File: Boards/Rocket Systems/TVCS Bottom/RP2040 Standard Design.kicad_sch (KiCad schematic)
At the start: 40 parts, among them J2 BM03B-SRSS-TBLFSN, J4 DX07S016JA1R1500, U1 ST1L05APU33R, U2 W25Q128JVSIQ TR, U3 ESD7L5.0DT5G

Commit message: Repo Refactor and new systems update
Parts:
- removed CV31, CV35: 1uF, Capacitor_0402:Capacitor_0402, symbol Device:C
- removed CV32, CV36: 100nF, Capacitor_0402:Capacitor_0402, symbol Device:C
- removed CV33, CV34: 4.7uF, C_4uF7_0402:C_4uF7_0402, symbol Device:C
- removed D1: PMEG2010ER, PMEG2010ER:SODFL3517X110N, symbol Schottky Diode:PMEG2010ER
- removed J2: BM03B-SRSS-TBLFSN, SWD_Con:CONN_BM03B-SRSS-TBLFSN_JST, symbol SWD Connector:BM03B-SRSS-TBLFSN
- removed J4: DX07S016JA1R1500, USBC-DX07S016JA1:JAE_DX07S016JA1R1500, symbol DX07S016JA1R1500:DX07S016JA1R1500
- removed R1, R10, R17: 1k, RES_0402:RES_0402, symbol Device:R
- removed R16: 10k, RES_0402:RES_0402, symbol Device:R
- removed R18, RC2: 5k1, R_0805_5K1:R_0805_5K1, symbol Device:R
- removed R2: 650, RC0402N_VIS:RC0402N_VIS, symbol Device:R
- removed R6, R7: 27, RES_R0603_27:RES_R0603_27, symbol Device:R
- removed R8, R9: 100, RES_0402:RES_0402, symbol Device:R
- removed U1: ST1L05APU33R, LDO ST1L05A:DFN_5APU33R_STM, symbol LDO 5V 3V3:ST1L05APU33R
- removed U2: W25Q128JVSIQ TR, NOR Flash:SOIC_208MIL_WIN, symbol 16MB Flash Memory:W25Q128JVSIQ_TR
- removed U3: ESD7L5.0DT5G, ESD7L5-Diode:SOT-723_0P85X1P25_ONS, symbol ESD Diodes:ESD7L5.0DT5G
- removed XTAL1: ASE-12.000MHZ-LC-T, AS12MHz:ASE-3.2X2.5_ABR, symbol Powered Crystal:ASE-12.000MHZ-LC-T
- added CV13, CV17: 1uF, Capacitor_0402:Capacitor_0402, symbol Device:C
- added CV14, CV18: 100nF, Capacitor_0402:Capacitor_0402, symbol Device:C
- added CV15, CV16: 4.7uF, C_4uF7_0402:C_4uF7_0402, symbol Device:C
- added D2: PMEG2010ER, PMEG2010ER:SODFL3517X110N, symbol PMEG2010ER:PMEG2010ER
- added J16: DX07S016JA1R1500, DX07S016JA1R1500:JAE_DX07S016JA1R1500, symbol DX07S016JA1R1500:DX07S016JA1R1500
- added J7: BM03B-SRSS-TBLFSN, CONN_BM03B-SRSS-TBLFSN_JST, symbol SWD_Con:BM03B-SRSS-TBLFSN
- added R22, R23: 27, RES_R0603_27:RES_R0603_27, symbol Device:R
- added R24, R25: 100, RES_0402:RES_0402, symbol Device:R
- added R26, R3, R35: 1k, RES_0402:RES_0402, symbol Device:R
- added R29: 10k, RES_0402:RES_0402, symbol Device:R
- added R30: 650, symbol Device:R
- added R33, R36: 5k1, R_0805_5K1:R_0805_5K1, symbol Device:R
- added U2: W25Q128JVSIQ TR, SOIC_208MIL_WIN, symbol 16MB_Flash:W25Q128JVSIQ_TR
- added U6: ESD7L5.0DT5G, SOT-723_0P85X1P25_ONS, symbol ESD7L5_Diode:ESD7L5.0DT5G
- added U7: ST1L05APU33R, DFN_5APU33R_STM, symbol LDO_ST1L05A:ST1L05APU33R
- added XTAL1: ASE-12.000MHZ-LC-T, ASE-3.2X2.5_ABR, symbol AS12MHz:ASE-12.000MHZ-LC-T
- S1, S2: footprint E-Switch_7mm:SW_TL3305CF160QG -> TL3305CF160QG:SW_TL3305CF160QG
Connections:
- net +3.3V: now also CV13.1, CV14.1, CV16.2, CV18.1, R29.2, R3.1, U2.8 (VCC), U7.2 (V0), XTAL1.4 (VDD)
- net +5V: now also CV15.2, CV17.2, D2.C, U7.3 (V1)
- net CRYSTAL: now also XTAL1.3 (OUTPUT)
- net GND: now also CV13.2, CV14.2, CV15.1, CV16.1, CV17.1, CV18.2, J16.1 (GND), J16.12 (GND), J7.2, R33.1, R36.1, U2.4 (GND), U6.3, U7.6 (GND), U7.7 (GND), XTAL1.2 (GND/CASE)
- net MCU QSPI_SCLK: now also U2.6 (CLK)
- net MCU QSPI_SD0: now also U2.5 (DI(IO0))
- net MCU QSPI_SD1: now also U2.2 (DO(IO1))
- net MCU QSPI_SD2: now also U2.3 (/WP(IO2))
- net MCU QSPI_SD3: now also U2.7 (/HOLD_/RESET)
- net MCU QSPI_SS: now also R35.2, U2.1 (/CS)
- net USB_DM: now also J16.5 (D-), J16.8 (D-), R23.1, U6.1
- net USB_DP: now also J16.6 (D+), J16.7 (D+), R22.1, U6.2
- net ~{RST}: now also S1.4, R26.1; no longer S2.4
- net ~{USB_BOOT}: now also S2.4, R35.1; no longer S1.4
- net at MCU1.47 (USB_DP): now also R22.2
- net at MCU1.25 (SWD): now also R25.2
- net at MCU1.24 (SWCLK): now also R24.2
- net at CV1.1, MCU1.26 (RUN): now also R26.2, R3.2
- net at CR1.2: now also R30.2
- net at MCU1.37 (GPIO25): now also R30.1
- net at MCU1.46 (USB_DM): now also R23.2
- net GP10/SPI1 SCK renamed GPIO10
- net GP11/SPI1 MOSI renamed GPIO11
- net GP17/SPI0 ~{CS} renamed GP17/SPI0 ~{CS2}
- net GP21/PWM2 B/CLKOUT 0 renamed GP21/SPI0 ~{CS3}
- net GP22/PWM3 A/CLKIN 1 renamed GPIO22
- net GP23/PWM3 B/CLKOUT 1 renamed GPIO23
- net GP3/UART0 RTS renamed GPIO3
- net GP4/UART1 TX renamed GPIO4
- net GP5/UART1 RX renamed GP5/SPI0 ~{CS1}
- net GP6/UART1 CTS renamed GPIO6
- net GP7/UART1 RTS renamed GPIO7
- net GP9/SPI1 ~{CS} renamed GPIO9
- new net: D2.A, J16.11 (VBUS), J16.2 (VBUS)
- new net: J16.3 (CC1), R36.2
- new net: J16.9 (CC2), R33.2
- new net: J16.S1 (SHIELD), J16.S2 (SHIELD), J16.S3 (SHIELD), J16.S4 (SHIELD), J16.S5 (SHIELD), J16.S6 (SHIELD)
- new net: J7.1, R24.1
- new net: J7.3, R25.1
- new net: R29.1, XTAL1.1 (TRI-STATE(STBY))

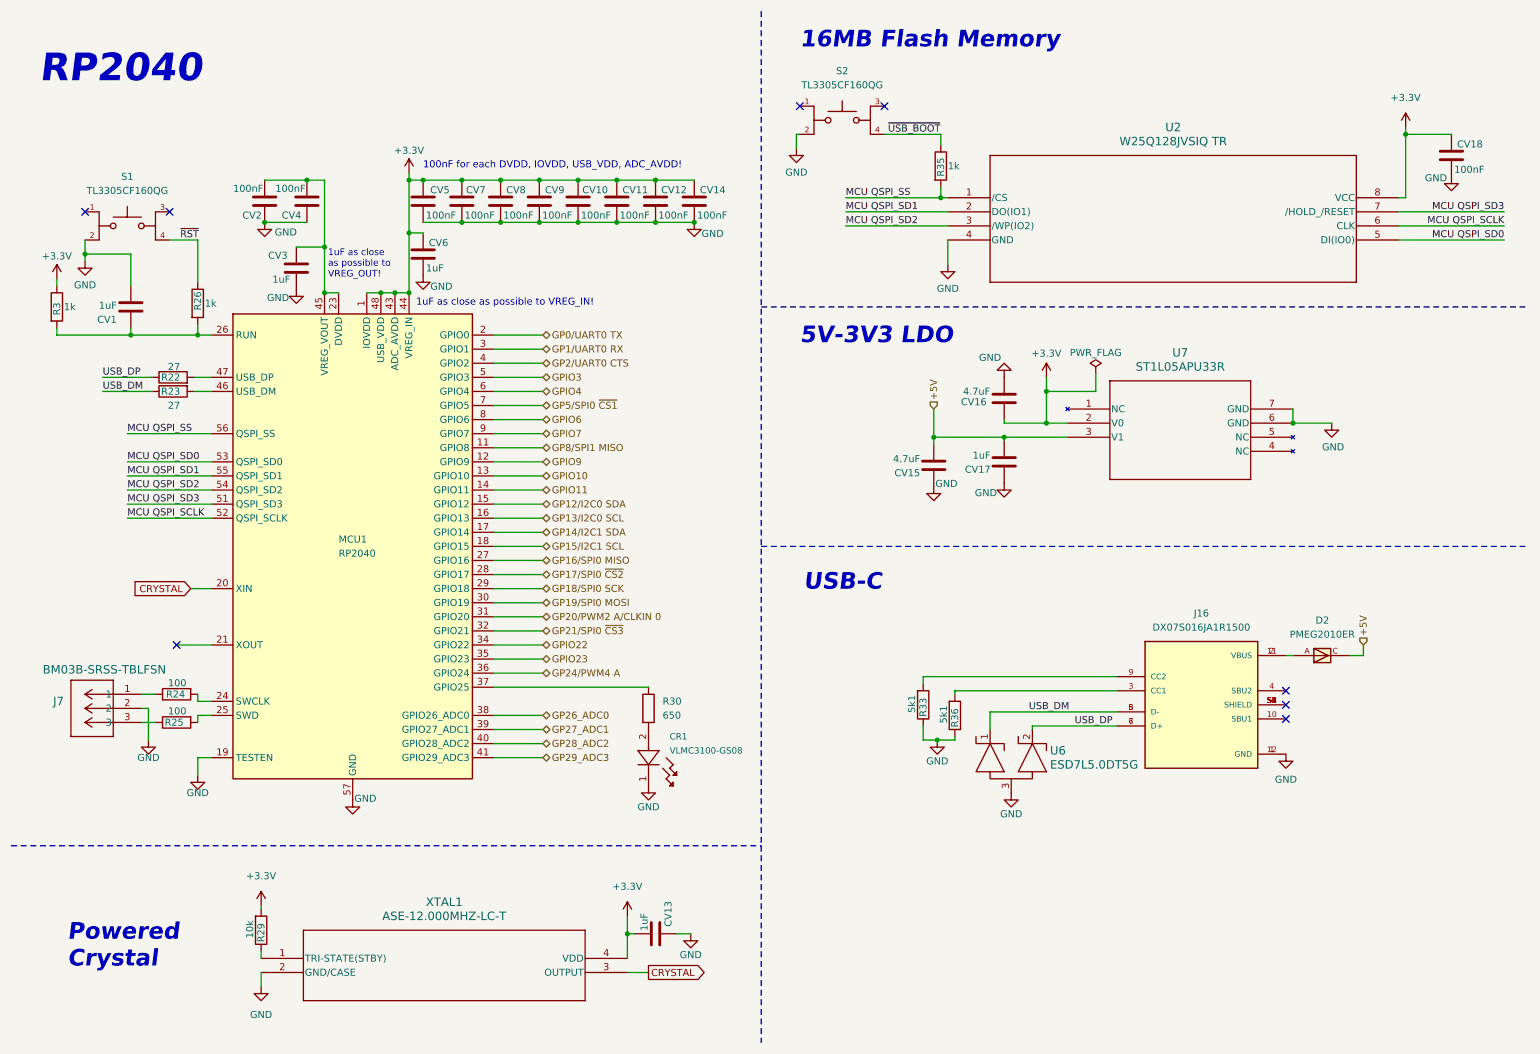
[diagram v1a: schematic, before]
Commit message: TVCS Top and Bottom
Footprints atualizadas
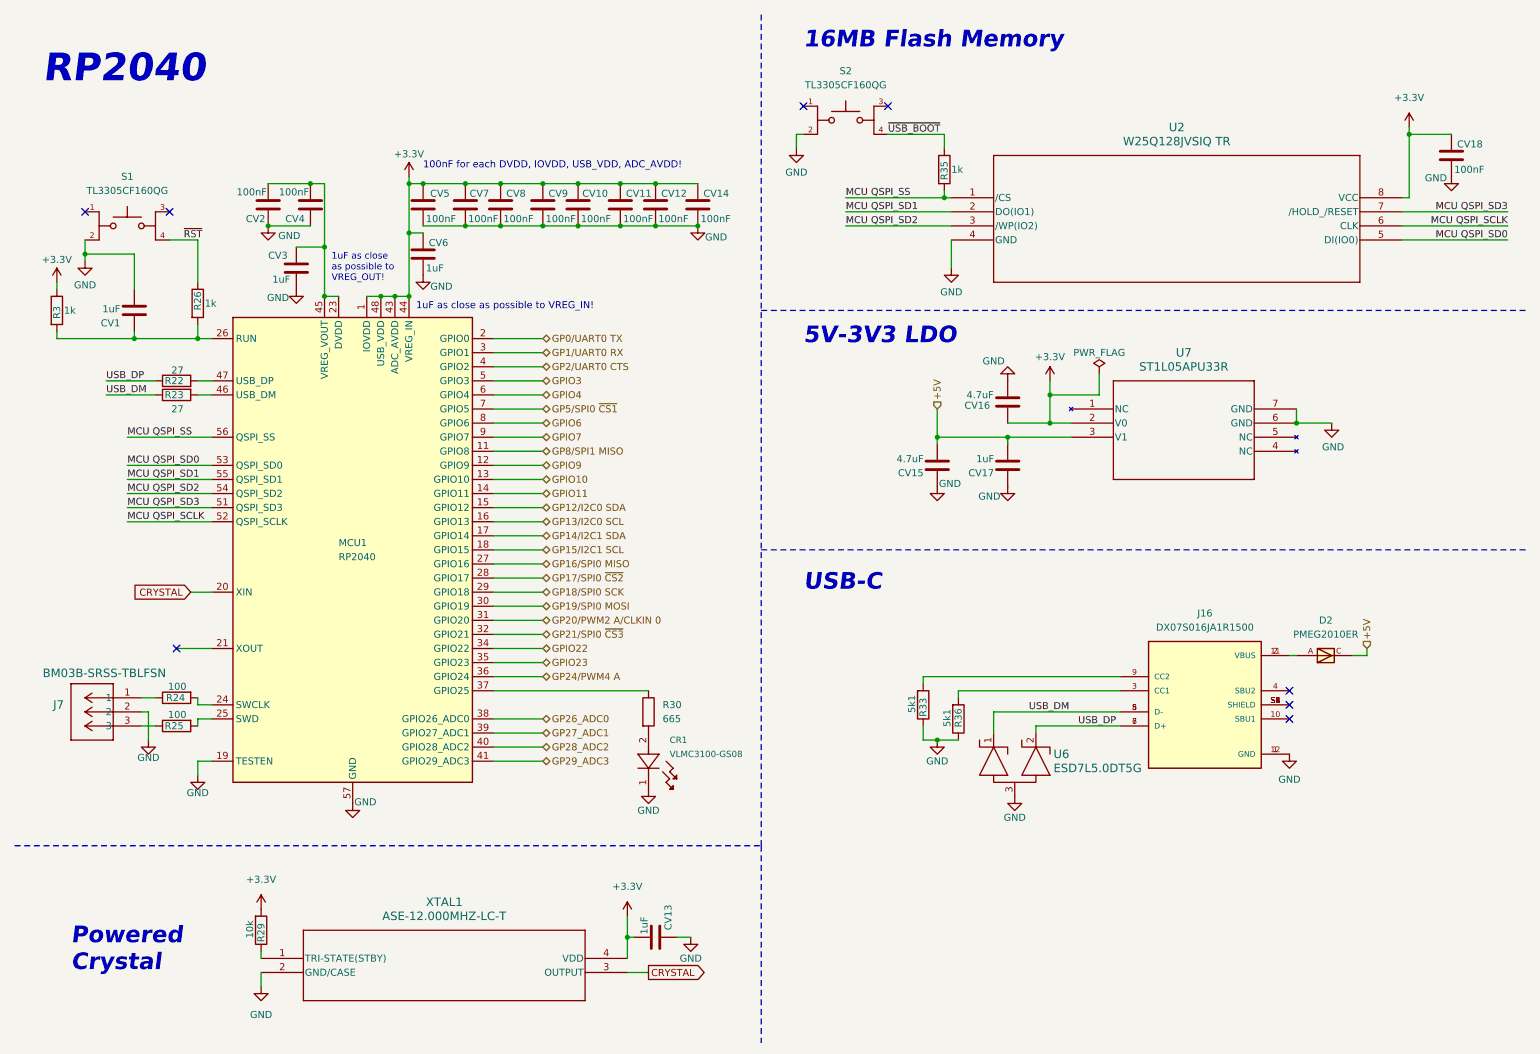
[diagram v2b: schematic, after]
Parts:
- CR1: footprint LED_PLCC_VSMB -> LED-Green_VLMC3100-GS08:LED_PLCC_VSMB
- CV1, CV10, CV11, CV12, CV13, CV14, CV17, CV18, CV2, CV3, CV4, CV5, CV6, CV7, CV8, CV9: footprint Capacitor_0402:Capacitor_0402 -> Capacitor-0402:Capacitor_0402
- CV15, CV16: footprint C_4uF7_0402:C_4uF7_0402 -> Capacitor-0402:Capacitor_0402
- D2: footprint PMEG2010ER:SODFL3517X110N -> Diode-Schottky_PMEG2010ER:SODFL3517X110N
- J16: footprint DX07S016JA1R1500:JAE_DX07S016JA1R1500 -> USBC-DX07S016JA1:JAE_DX07S016JA1R1500
- J7: footprint CONN_BM03B-SRSS-TBLFSN_JST -> SWD_Con:CONN_BM03B-SRSS-TBLFSN_JST
- R22, R23: footprint RES_R0603_27:RES_R0603_27 -> Resistor-0603:RES_0603
- R24, R25, R26, R29, R3, R35: footprint RES_0402:RES_0402 -> Resistor-0402:RES_0402
- R30: value 650 -> 665; footprint (none) -> Resistor-0402:RES_0402
- R33, R36: footprint R_0805_5K1:R_0805_5K1 -> Resistor-0805:RES_0805
- S1, S2: footprint TL3305CF160QG:SW_TL3305CF160QG -> E-Switch_7mm:SW_TL3305CF160QG
- U2: footprint SOIC_208MIL_WIN -> NOR Flash:SOIC_208MIL_WIN
- U6: footprint SOT-723_0P85X1P25_ONS -> ESD7L5-Diode:SOT-723_0P85X1P25_ONS
- U7: footprint DFN_5APU33R_STM -> LDO ST1L05A:DFN_5APU33R_STM
- XTAL1: footprint ASE-3.2X2.5_ABR -> AS12MHz:ASE-3.2X2.5_ABR

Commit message: Tu viste o q eu fiz
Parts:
- removed S1, S2: TL3305CF160QG, E-Switch_7mm:SW_TL3305CF160QG, symbol TL3305CF160QG:TL3305CF160QG
- added S1, S2: TL1017AABF160QG, E-Switch_Small:TL1017AABF160QG, symbol TL1017AABF160QG:TL1017AABF160QG
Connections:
- net GND: now also S1.1 (COM), S1.G1, S2.1 (COM), S2.G1
- net ~{RST}: now also S1.2 (NO)
- net ~{USB_BOOT}: now also S2.2 (NO)
- no-connect marks 8 -> 4

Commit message: Communication boards update
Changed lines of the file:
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@@
 	(wire
 		(pts
-			(xy 256.54 128.27) (xy 254 128.27)
+			(xy 258.445 128.27) (xy 254 128.27)
 		)
 		(stroke
@@
 	(wire
 		(pts
-			(xy 256.54 127) (xy 256.54 128.27)
+			(xy 258.445 127) (xy 258.445 128.27)
 		)
 		(stroke
@@
 	(label "MCU QSPI_SS"
 		(at 33.02 88.9 0)
-		(fields_autoplaced yes)
 		(effects
 			(font
@@
 	(label "MCU QSPI_SD3"
 		(at 33.02 101.6 0)
-		(fields_autoplaced yes)
 		(effects
 			(font
@@
 	(label "MCU QSPI_SD1"
 		(at 162.56 48.26 0)
-		(fields_autoplaced yes)
 		(effects
 			(font
@@
 	(label "MCU QSPI_SD0"
 		(at 33.02 93.98 0)
-		(fields_autoplaced yes)
 		(effects
 			(font
@@
 	(label "USB_DM"
 		(at 29.21 81.28 0)
-		(fields_autoplaced yes)
 		(effects
 			(font
@@
 	(label "~{RST}"
 		(at 43.18 52.07 0)
-		(fields_autoplaced yes)
 		(effects
 			(font
@@
 	(label "MCU QSPI_SD2"
 		(at 33.02 99.06 0)
-		(fields_autoplaced yes)
 		(effects
 			(font
@@
 	(label "MCU QSPI_SD3"
 		(at 281.94 48.26 180)
-		(fields_autoplaced yes)
 		(effects
 			(font
@@
 	(label "USB_DM"
 		(at 195.58 138.43 0)
-		(fields_autoplaced yes)
 		(effects
 			(font
@@
 	(label "MCU QSPI_SD0"
 		(at 281.94 53.34 180)
-		(fields_autoplaced yes)
 		(effects
 			(font
@@
 	(label "MCU QSPI_SCLK"
 		(at 281.94 50.8 180)
-		(fields_autoplaced yes)
 		(effects
 			(font
@@
 	(label "USB_DP"
 		(at 29.21 78.74 0)
-		(fields_autoplaced yes)
 		(effects
 			(font
@@
 	(label "MCU QSPI_SS"
 		(at 162.56 45.72 0)
-		(fields_autoplaced yes)
 		(effects
 			(font
@@
 	(label "MCU QSPI_SD1"
 		(at 33.02 96.52 0)
-		(fields_autoplaced yes)
 		(effects
 			(font
@@
 	(label "MCU QSPI_SD2"
 		(at 162.56 50.8 0)
-		(fields_autoplaced yes)
 		(effects
 			(font
@@
 	(label "~{USB_BOOT}"
 		(at 170.18 34.29 0)
-		(fields_autoplaced yes)
 		(effects
 			(font
@@
 	(label "USB_DP"
 		(at 204.47 140.97 0)
-		(fields_autoplaced yes)
 		(effects
 			(font
@@
 	(label "MCU QSPI_SCLK"
 		(at 33.02 104.14 0)
-		(fields_autoplaced yes)
 		(effects
 			(font
@@
 		(shape bidirectional)
 		(at 107.95 142.24 0)
-		(fields_autoplaced yes)
 		(effects
 			(font
@@
 		(shape bidirectional)
 		(at 107.95 96.52 0)
-		(fields_autoplaced yes)
 		(effects
 			(font
@@
 		(shape bidirectional)
 		(at 107.95 106.68 0)
-		(fields_autoplaced yes)
 		(effects
 			(font
@@
 		(shape bidirectional)
 		(at 107.95 83.82 0)
-		(fields_autoplaced yes)
 		(effects
 			(font
@@
 		(shape bidirectional)
 		(at 107.95 147.32 0)
-		(fields_autoplaced yes)
 		(effects
 			(font
@@
 		(shape bidirectional)
 		(at 107.95 76.2 0)
-		(fields_autoplaced yes)
 		(effects
 			(font
@@
 		(shape bidirectional)
 		(at 107.95 71.12 0)
-		(fields_autoplaced yes)
 		(effects
 			(font
@@
 		(shape bidirectional)
 		(at 107.95 119.38 0)
-		(fields_autoplaced yes)
 		(effects
 			(font
@@
 		(shape bidirectional)
 		(at 107.95 124.46 0)
-		(fields_autoplaced yes)
 		(effects
 			(font
@@
 		(shape bidirectional)
 		(at 107.95 93.98 0)
-		(fields_autoplaced yes)
 		(effects
 			(font
@@
 		(shape bidirectional)
 		(at 107.95 88.9 0)
-		(fields_autoplaced yes)
 		(effects
 			(font
@@
 		(shape bidirectional)
 		(at 107.95 101.6 0)
-		(fields_autoplaced yes)
 		(effects
 			(font
@@
 		(shape input)
 		(at 179.07 83.82 90)
-		(fields_autoplaced yes)
 		(effects
 			(font
@@
 		(shape bidirectional)
 		(at 107.95 73.66 0)
-		(fields_autoplaced yes)
 		(effects
 			(font
@@
 		(shape bidirectional)
 		(at 107.95 129.54 0)
-		(fields_autoplaced yes)
 		(effects
 			(font
@@
 		(shape bidirectional)
 		(at 107.95 144.78 0)
-		(fields_autoplaced yes)
 		(effects
 			(font
@@
 		(shape bidirectional)
 		(at 107.95 86.36 0)
-		(fields_autoplaced yes)
 		(effects
 			(font
@@
 		(shape bidirectional)
 		(at 107.95 121.92 0)
-		(fields_autoplaced yes)
 		(effects
 			(font
@@
 		(shape bidirectional)
 		(at 107.95 109.22 0)
-		(fields_autoplaced yes)
 		(effects
 			(font
@@
 		(shape bidirectional)
 		(at 107.95 127 0)
-		(fields_autoplaced yes)
 		(effects
 			(font
@@
 		(shape bidirectional)
 		(at 107.95 91.44 0)
-		(fields_autoplaced yes)
 		(effects
 			(font
@@
 		(shape bidirectional)
 		(at 107.95 78.74 0)
-		(fields_autoplaced yes)
 		(effects
 			(font
@@
 		(shape bidirectional)
 		(at 107.95 132.08 0)
-		(fields_autoplaced yes)
 		(effects
 			(font
@@
 		(shape bidirectional)
 		(at 107.95 104.14 0)
-		(fields_autoplaced yes)
 		(effects
 			(font
@@
 		(shape bidirectional)
 		(at 107.95 111.76 0)
-		(fields_autoplaced yes)
 		(effects
 			(font
@@
 		(shape bidirectional)
 		(at 107.95 81.28 0)
-		(fields_autoplaced yes)
 		(effects
 			(font
@@
 		(shape bidirectional)
 		(at 107.95 99.06 0)
-		(fields_autoplaced yes)
 		(effects
 			(font
@@
 	(hierarchical_label "+5V"
 		(shape input)
-		(at 256.54 127 90)
-		(fields_autoplaced yes)
+		(at 258.445 127 90)
 		(effects
 			(font
@@
 		(shape bidirectional)
 		(at 107.95 139.7 0)
-		(fields_autoplaced yes)
 		(effects
 			(font
@@
 		(shape bidirectional)
 		(at 107.95 116.84 0)
-		(fields_autoplaced yes)
 		(effects
 			(font
@@
 		(shape bidirectional)
 		(at 107.95 114.3 0)
-		(fields_autoplaced yes)
-		(effects
-			(font
+		(effects
+			(font
